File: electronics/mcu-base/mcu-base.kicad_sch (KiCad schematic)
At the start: 7 parts

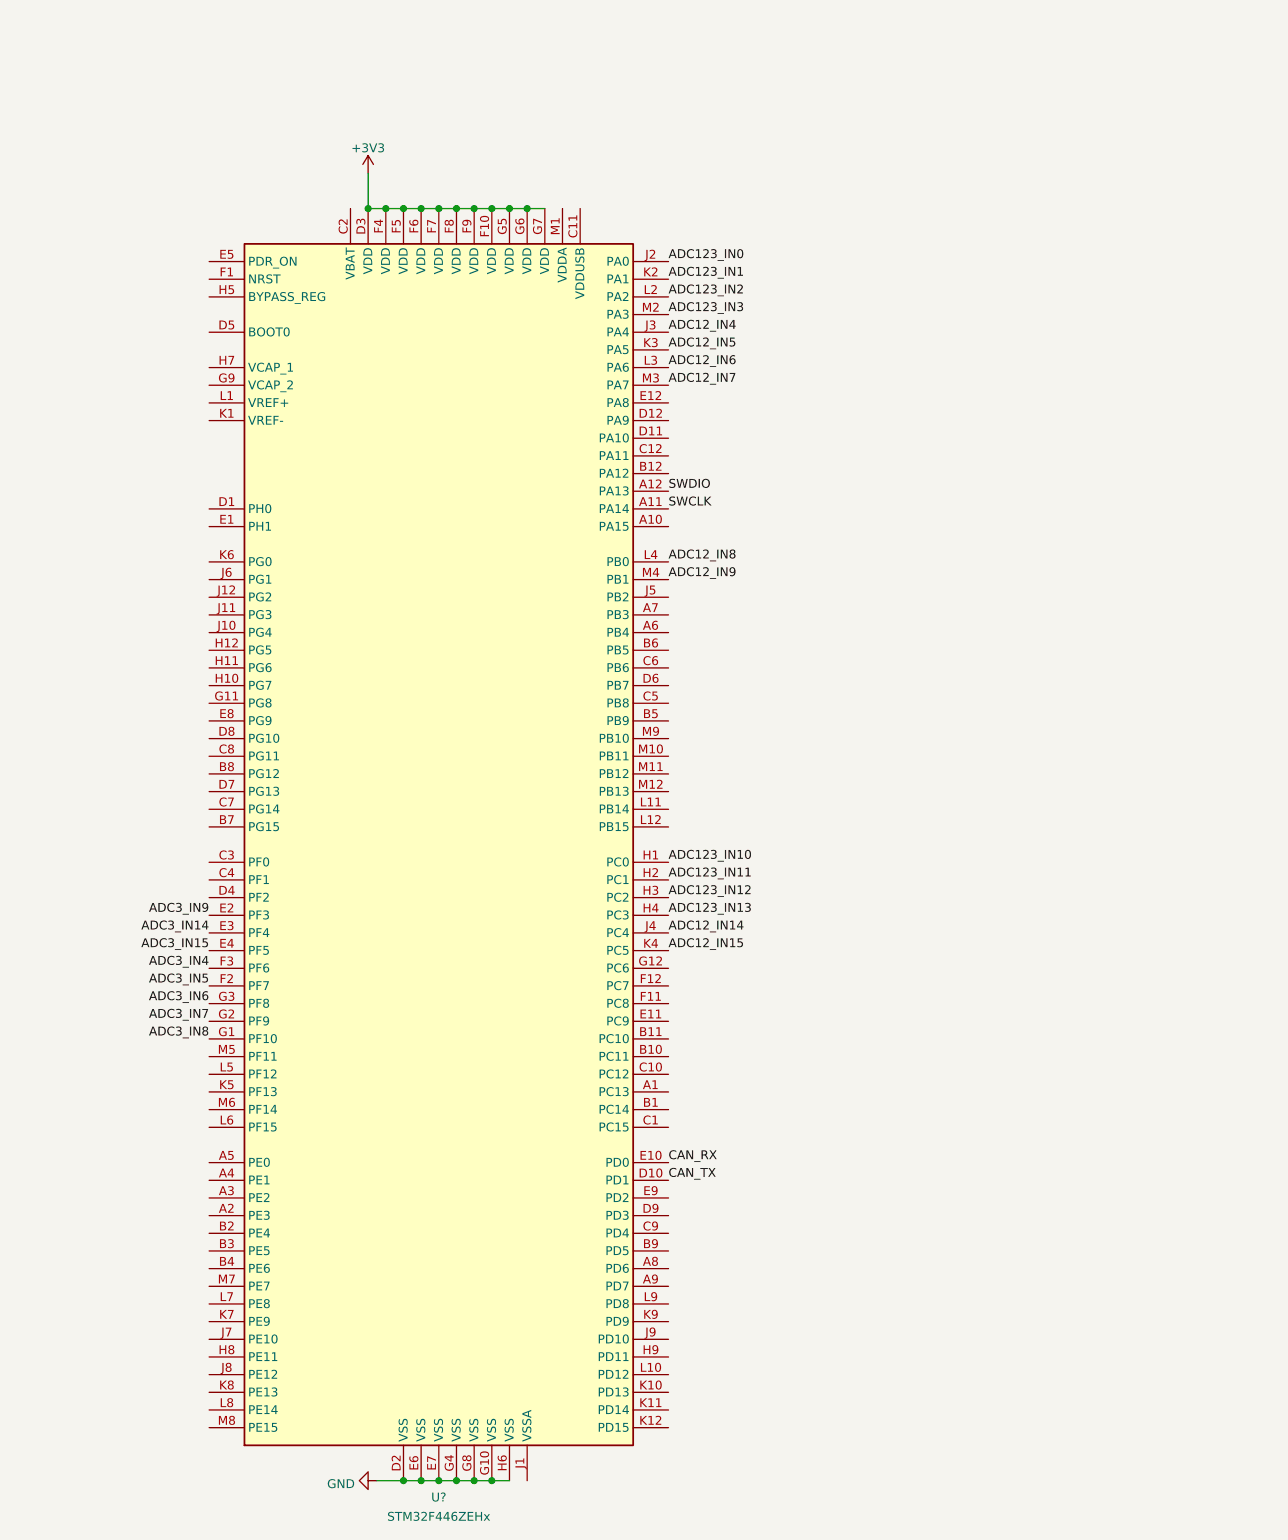
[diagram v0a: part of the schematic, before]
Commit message: Add oscillators and some various stuff around the stm32 to the mcu-base
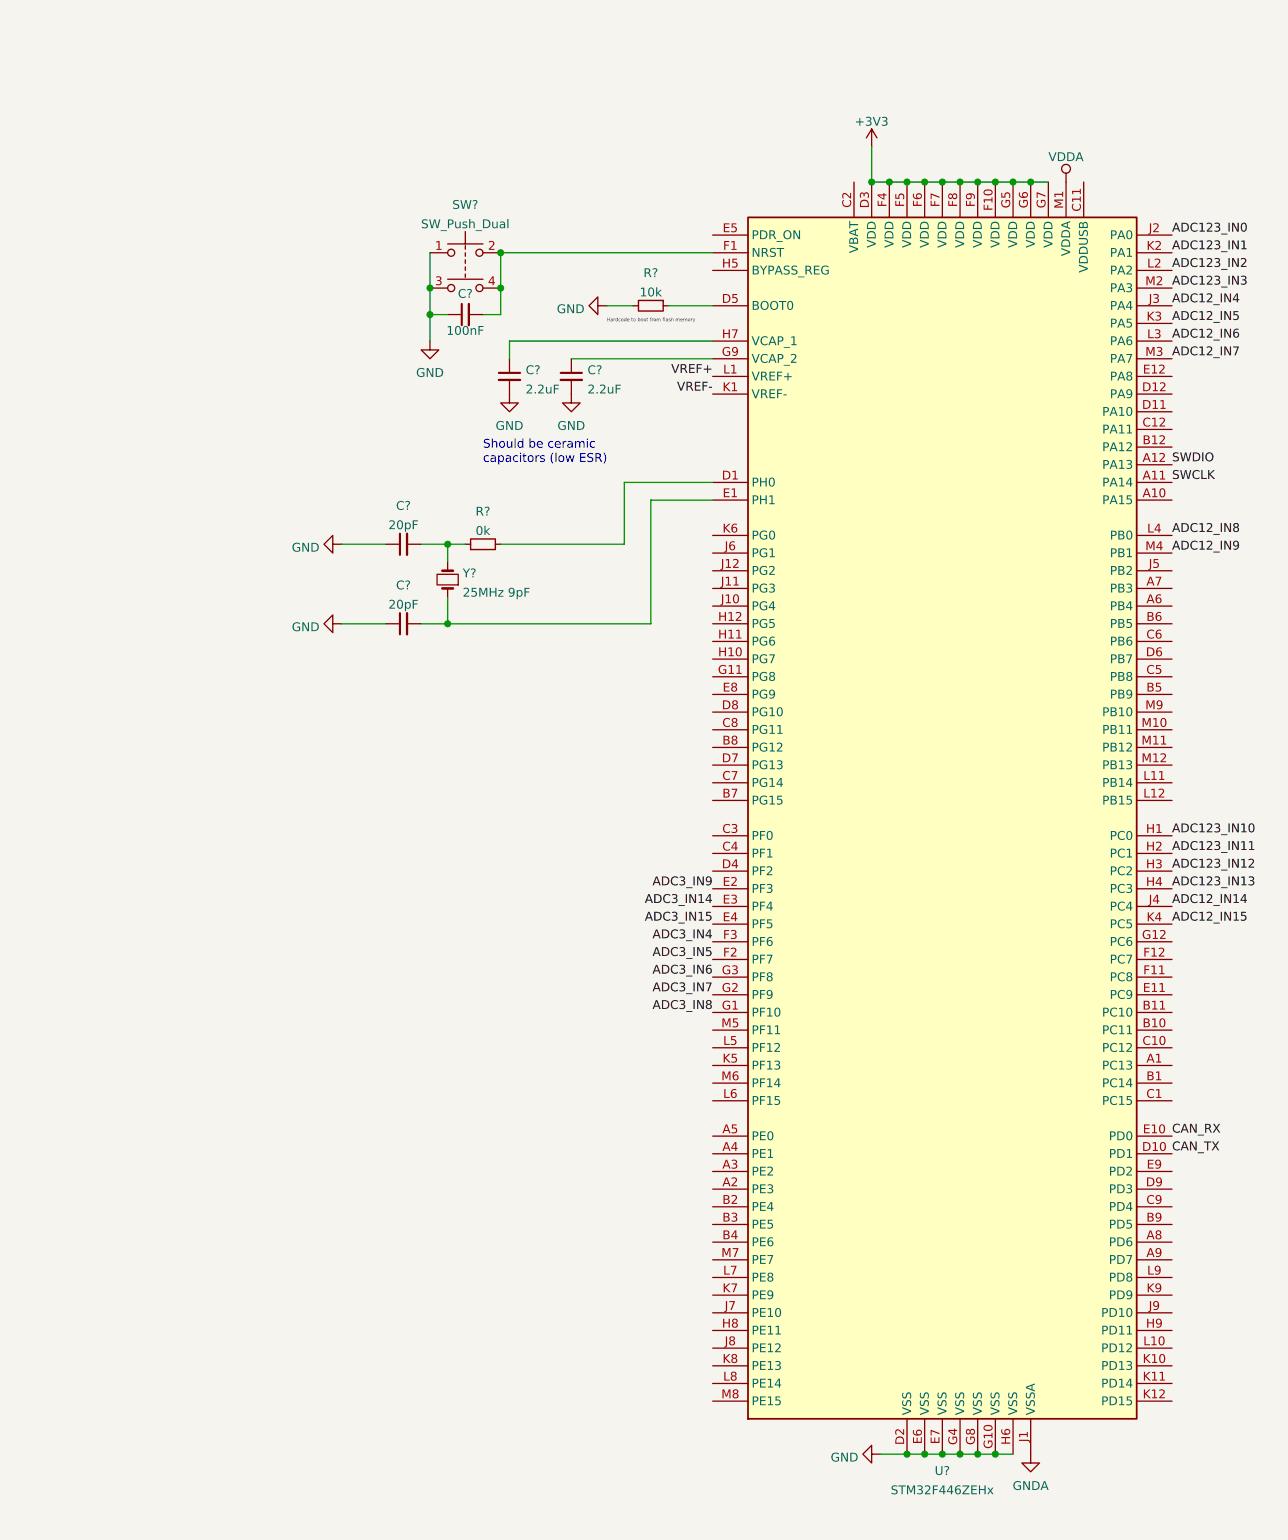
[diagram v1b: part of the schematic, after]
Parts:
- added C? (x2): 20pF, symbol Device:C_Small
- added C? (x2): 2.2uF, symbol Device:C_Small
- added C?: 100nF, symbol Device:C_Small
- added R?: 10k, symbol Device:R_Small
- added R?: 0k, symbol Device:R_Small
- added SW?: SW_Push_Dual, symbol Switch:SW_Push_Dual
- added Y?: 25MHz 9pF, symbol Device:Crystal_Small
- J?: footprint (none) -> Connector_PinHeader_2.54mm:PinHeader_1x04_P2.54mm_Vertical
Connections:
- net GND: now also C?.1, C?.1, C?.1, C?.2, C?.2, R?.2, SW?.1, SW?.3
- net at U?.D1 (PH0): now also R?.2
- net at U?.D5 (BOOT0): now also R?.1
- net at U?.E1 (PH1): now also C?.2, Y?.1
- net at U?.F1 (NRST): now also C?.2, SW?.2, SW?.4
- net at U?.G9 (VCAP_2): now also C?.1
- net at U?.H7 (VCAP_1): now also C?.1
- net GNDA: now reaches U?.J1 (VSSA)
- net VREF-: now reaches U?.K1 (VREF-)
- net VREF+: now reaches U?.L1 (VREF+)
- net VDDA: now reaches U?.M1 (VDDA)
- new net: C?.2, R?.1, Y?.2
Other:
- note added: "Hardcode to boot from flash memory"
- note added: "Should be ceramic capacitors (low ESR)"
- moved on the sheet: U?

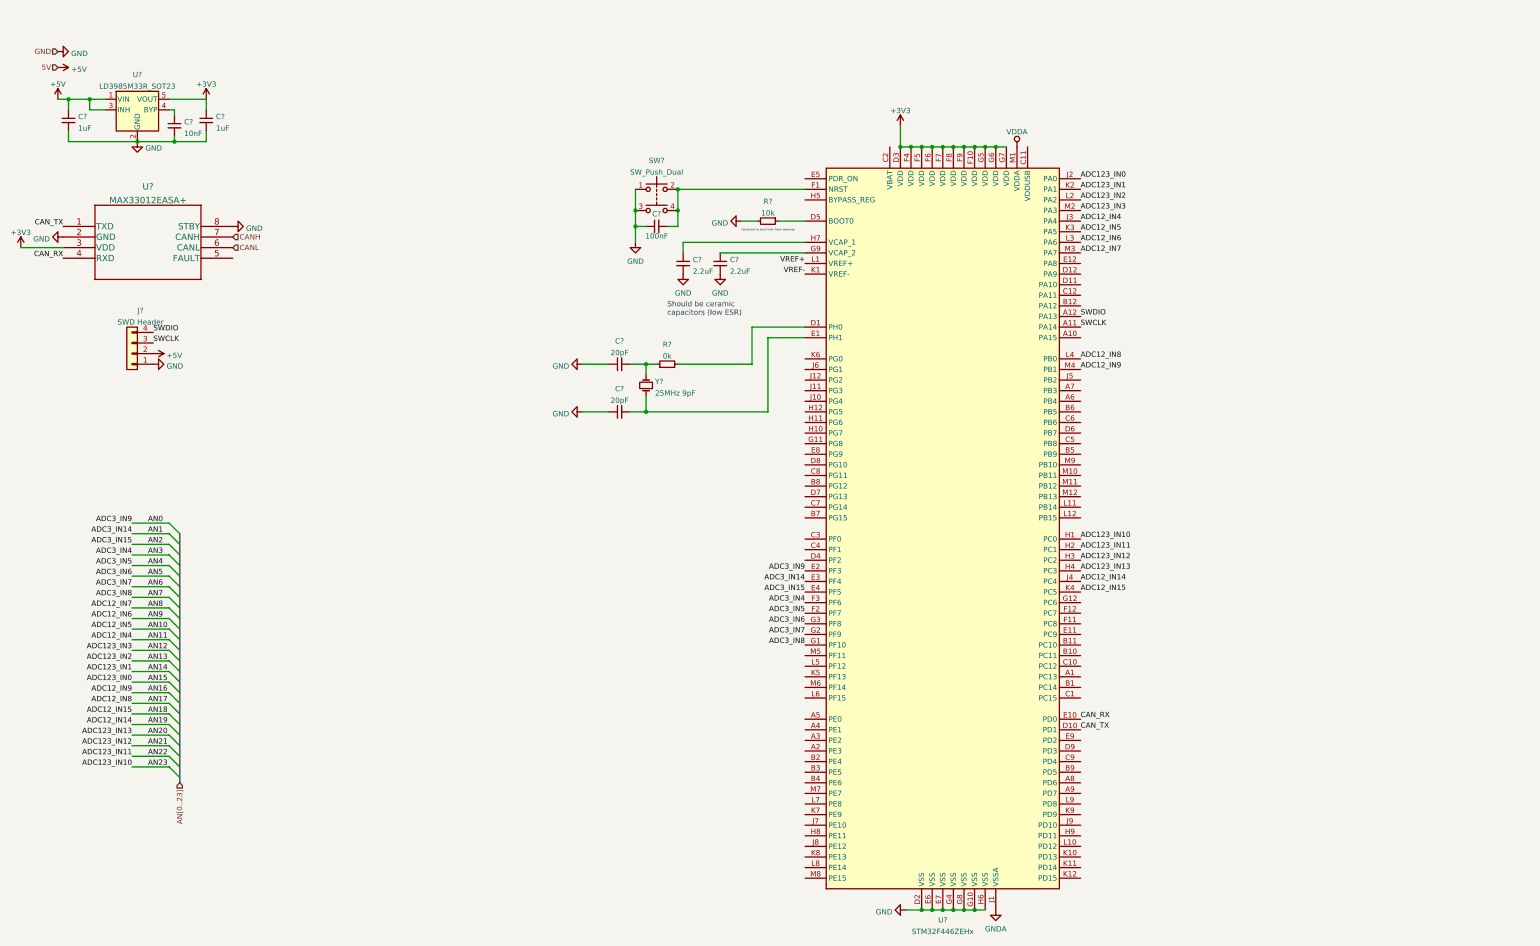
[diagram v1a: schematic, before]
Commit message: Remove hiearchy from mcu-base
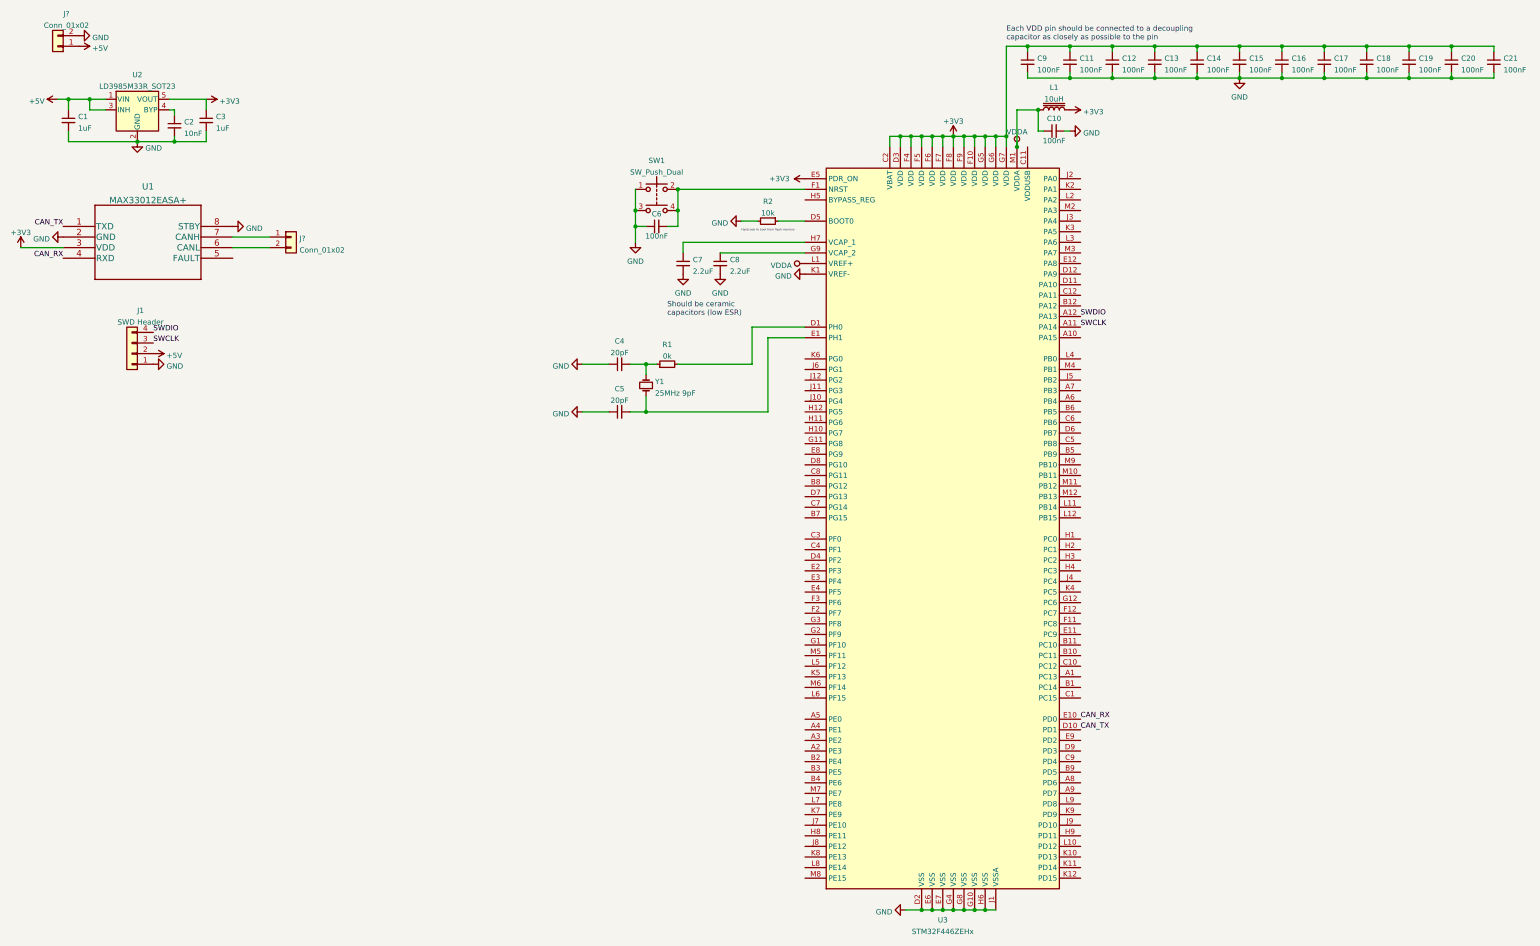
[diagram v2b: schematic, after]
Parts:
- added C10, C11, C12, C13, C14, C15, C16, C17, C18, C19, C20, C21, C9: 100nF, symbol Device:C_Small
- added J? (x2): Conn_01x02, symbol Connector_Generic:Conn_01x02
- added L1: 10uH, symbol Device:L_Core_Iron
- gave numbers to parts that had none: 16
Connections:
- net GNDA is gone; now on net GND: U3.J1 (VSSA)
- net VREF+ is gone; now on net VDDA: U3.L1 (VREF+)
- net VREF- is gone; now on net GND: U3.K1 (VREF-)
- net +3V3: now also U3.C2 (VBAT), U3.E5 (PDR_ON), C11.1, C12.1, C13.1, C14.1, C15.1, C16.1, C17.1, C18.1, C19.1, C20.1, C21.1, C9.1, L1.2
- net +5V: now also J?.1 (Pin_1)
- net GND: now also C10.2, C11.2, C12.2, C13.2, C14.2, C15.2, C16.2, C17.2, C18.2, C19.2, C20.2, C21.2, C9.2, J?.2 (Pin_2)
- net VDDA: now also C10.1, L1.1
- net ADC123_IN0: no longer names the net of U3.J2 (PA0)
- net ADC123_IN1: no longer names the net of U3.K2 (PA1)
- net ADC123_IN10: no longer names the net of U3.H1 (PC0)
- net ADC123_IN11: no longer names the net of U3.H2 (PC1)
- net ADC123_IN12: no longer names the net of U3.H3 (PC2)
- net ADC123_IN13: no longer names the net of U3.H4 (PC3)
- net ADC123_IN2: no longer names the net of U3.L2 (PA2)
- net ADC123_IN3: no longer names the net of U3.M2 (PA3)
- net ADC12_IN14: no longer names the net of U3.J4 (PC4)
- net ADC12_IN15: no longer names the net of U3.K4 (PC5)
- net ADC12_IN4: no longer names the net of U3.J3 (PA4)
- net ADC12_IN5: no longer names the net of U3.K3 (PA5)
- net ADC12_IN6: no longer names the net of U3.L3 (PA6)
- net ADC12_IN7: no longer names the net of U3.M3 (PA7)
- net ADC12_IN8: no longer names the net of U3.L4 (PB0)
- net ADC12_IN9: no longer names the net of U3.M4 (PB1)
- net ADC3_IN14: no longer names the net of U3.E3 (PF4)
- net ADC3_IN15: no longer names the net of U3.E4 (PF5)
- net ADC3_IN4: no longer names the net of U3.F3 (PF6)
- net ADC3_IN5: no longer names the net of U3.F2 (PF7)
- net ADC3_IN6: no longer names the net of U3.G3 (PF8)
- net ADC3_IN7: no longer names the net of U3.G2 (PF9)
- net ADC3_IN8: no longer names the net of U3.G1 (PF10)
- net ADC3_IN9: no longer names the net of U3.E2 (PF3)
- net CANH: no longer names the net of U1.7 (CANH)
- net CANH: now also J?.1 (Pin_1)
- net CANL: no longer names the net of U1.6 (CANL)
- net CANL: now also J?.2 (Pin_2)
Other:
- note added: "Each VDD pin should be connected to a decoupling capacitor as closely as possible to the pin"

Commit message: Put in connectors and finalized layout of everything except MCU.
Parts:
- removed C13, C14, C15, C16, C17, C18, C19, C20, C21: 100nF, symbol Device:C_Small
- added C? (x2): 100nF, symbol Device:C_Small
- added U4: STM32L051R6Tx, Package_QFP:LQFP-64_10x10mm_P0.5mm, symbol MCU_ST_STM32L0:STM32L051R6Tx
- gave numbers to parts that had none: 2
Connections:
- net +3V3: now also C?.1, C?.1, U4.1 (VLCD), U4.19 (VDD), U4.32 (VDD), U4.48 (VDDIO2), U4.64 (VDD); no longer U3.C2 (VBAT), U3.D3 (VDD), U3.F10 (VDD), U3.F4 (VDD), U3.F5 (VDD), U3.F6 (VDD), U3.F7 (VDD), U3.F8 (VDD), U3.F9 (VDD), U3.G5 (VDD), U3.G6 (VDD), U3.G7 (VDD)
- net GND: now also C?.2, C?.2, U4.12 (VSSA), U4.18 (VSS), U4.31 (VSS), U4.47 (VSS), U4.63 (VSS); no longer U3.D2 (VSS), U3.E6 (VSS), U3.E7 (VSS), U3.G10 (VSS), U3.G4 (VSS), U3.G8 (VSS), U3.H6 (VSS), U3.J1 (VSSA)
- net SWCLK: now also U4.49 (PA14); no longer U3.A11 (PA14)
- net SWDIO: now also U4.46 (PA13); no longer U3.A12 (PA13)
- net VDDA: now also U4.13 (VDDA); no longer U3.M1 (VDDA)
- net at R2.1: now also U4.60 (BOOT0); no longer U3.D5 (BOOT0)
- net at U3.D1 (PH0): no longer R1.2
- net at C5.2, Y1.1: now also U4.6 (PH1); no longer U3.E1 (PH1)
- net at C6.2, SW1.2, SW1.4: now also U4.7 (NRST); no longer U3.F1 (NRST)
- new net: R1.2, U4.5 (PH0)
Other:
- moved on the sheet: C7, C8, U3

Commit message: Updated MCU Base and started MCU on Output Board
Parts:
- removed C7, C8: 2.2uF, symbol Device:C_Small
- removed U3: STM32F446ZEHx, Package_BGA:UFBGA-144_7x7mm_Layout12x12_P0.5mm, symbol MCU_ST_STM32F4:STM32F446ZEHx
- removed U4: STM32L051R6Tx, Package_QFP:LQFP-64_10x10mm_P0.5mm, symbol MCU_ST_STM32L0:STM32L051R6Tx
- added C13: 100nF, Capacitor_SMD:C_0603_1608Metric, symbol Device:C_Small
- added U3: STM32F105VBH6, Package_BGA:LFBGA-100_10x10mm_Layout10x10_P0.8mm, symbol F105 MCU:STM32F105VBH6
- C1: footprint (none) -> Package_BGA:LFBGA-100_10x10mm_Layout10x10_P0.8mm
- C10, C11, C12, C2, C3, C4, C5, C6, C9: footprint (none) -> Capacitor_SMD:C_0603_1608Metric
- C7, C8: renamed from C?; footprint (none) -> Capacitor_SMD:C_0603_1608Metric
- J2: value Conn_01x02 -> 5V In; footprint (none) -> CustomFootprints:LatchingConnector2POS
- J3: value Conn_01x02 -> CAN IN; footprint (none) -> CustomFootprints:LatchingConnector2POS
- L1: footprint (none) -> Inductor_SMD:L_0603_1608Metric
- R1, R2: footprint (none) -> Resistor_SMD:R_0603_1608Metric
- SW1: footprint (none) -> Button:Button CS1102
- U1: footprint 21-0041-3-M_90-0096-8L_MXM -> MAX33012EASA+:MAX33012EASA+
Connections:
- net +3V3: now also C13.1, U3.B2 (VBAT), U3.D2 (VDD_5), U3.F4 (VDD_4), U3.F5 (VDD_3), U3.F6 (VDD_2), U3.F7 (VDD_1)
- net CAN_RX: now also U3.C10 (PA11)
- net CAN_TX: now also U3.B10 (PA12)
- net GND: now also C6.2, SW1.2, SW1.4, C13.2, U3.C2 (VSS_5), U3.E4 (VSS_4), U3.E5 (VSS_3), U3.E6 (VSS_2), U3.E7 (VSS_1), U3.G1 (VSSA), U3.H1 (VREF-); no longer C6.1, SW1.1, SW1.3
- net SWCLK: now also U3.A9 (PA14)
- net SWDIO: now also U3.A10 (PA13)
- net VDDA: now also U3.J1 (VREF+), U3.K1 (VDDA)
- net at C5.2, Y1.1: now also U3.C1 (OSC_IN)
- net at R2.1: now also U3.D5 (BOOT0)
- net at R1.2: now also U3.D1 (OSC_OUT)
- new net: C6.1, SW1.1, SW1.3, U3.E1 (NRST)
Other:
- note removed: "Should be ceramic capacitors (low ESR)"
- moved on the sheet: C10, C11, C12, C4, C5, C6, C7, C8, C9, L1, R1, R2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
